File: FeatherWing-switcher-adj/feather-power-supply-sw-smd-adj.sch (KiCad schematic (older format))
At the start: 31 parts, among them J1 Conn_01x12, J2 Conn_01x16, J3 QWIIC, J4 0.1\"x4, J5 5.08mm, Q1 Q_PMOS_GSD, U1 MCP16312MS

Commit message: minor board changes
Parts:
- C2, C3: Voltage (none) -> 35V
- C5, C6: Voltage (none) -> 6.3V
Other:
- moved on the sheet: F1
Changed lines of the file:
@@
 Comment2 "All capacitors are 0603 X7R class unless noted. C2,C3,C5,C6 are 1206, low esr"
 Comment3 "All resistors are 1% 0603"
-Comment4 "Purple text indicate DigiKey part numbers"
+Comment4 "Purple text indicate Digi-Key part numbers"
 $EndDescr
 $Comp
@@
 F 2 "Connector_JST:JST_SH_SM04B-SRSS-TB_1x04-1MP_P1.00mm_Horizontal" H 3300 4750 50  0001 C CNN
 F 3 "https://cdn-shop.adafruit.com/product-files/4328/4328_C13916-001_CCSH-W10-04-BK-RC-A.pdf" H 3300 4750 50  0001 C CNN
-F 4 "455-1804-1-ND" H 3290 5040 30  0000 C CNN "DigiKey_PN"
+F 4 "455-1804-1-ND" H 3290 5040 30  0001 C CNN "DigiKey_PN"
 	1    3300 4750
 	-1   0    0    1
@@
 L Device:Polyfuse_Small F1
 U 1 1 5F5C90E5
-P 3450 2100
-F 0 "F1" V 3550 2100 50  0000 C CNN
-F 1 "24V 1.1A" V 3564 2100 50  0001 C CNN
-F 2 "Fuse:Fuse_1812_4532Metric_Castellated" H 3500 1900 50  0001 L CNN
-F 3 "~" H 3450 2100 50  0001 C CNN
-F 4 "F5632CT-ND" V 3360 2140 30  0001 C CNN "DigiKey-PN"
-F 5 "1812L110/24DR" V 3450 2100 50  0001 C CNN "MPN"
-F 6 "Littelfuse Inc." V 3450 2100 50  0001 C CNN "LittleFuse"
-	1    3450 2100
+P 3475 2100
+F 0 "F1" V 3575 2100 50  0000 C CNN
+F 1 "24V 1.1A" V 3589 2100 50  0001 C CNN
+F 2 "Fuse:Fuse_1812_4532Metric_Castellated" H 3525 1900 50  0001 L CNN
+F 3 "~" H 3475 2100 50  0001 C CNN
+F 4 "F5632CT-ND" V 3385 2140 30  0001 C CNN "DigiKey-PN"
+F 5 "1812L110/24DR" V 3475 2100 50  0001 C CNN "MPN"
+F 6 "Littelfuse Inc." V 3475 2100 50  0001 C CNN "LittleFuse"
+	1    3475 2100
 	0    -1   -1   0
 $EndComp
@@
 U 1 1 5F8EC01A
 P 5000 2200
-F 0 "R1" V 4850 2200 50  0000 C CNN
-F 1 "1M" V 4920 2200 50  0000 C CNN
+F 0 "R1" V 4925 2200 50  0000 C CNN
+F 1 "1M" V 4850 2200 50  0000 C CNN
 F 2 "Resistor_SMD:R_0603_1608Metric_Pad1.05x0.95mm_HandSolder" H 5000 2200 50  0001 C CNN
 F 3 "~" H 5000 2200 50  0001 C CNN
@@
 	3300 2000 3300 2100
 Wire Wire Line
-	3300 2100 3350 2100
-Wire Wire Line
-	3550 2100 3650 2100
+	3300 2100 3375 2100
+Wire Wire Line
+	3575 2100 3650 2100
 $Comp
 L Device:Q_PMOS_GSD Q1
@@
 F 6 "587-3007-1-ND" H 4350 2550 50  0001 C CNN "Digi-Key_PN"
 F 7 "Digi-Key" H 4350 2550 50  0001 C CNN "Vendor"
+F 8 "35V" H 4250 2350 50  0000 C CNN "Voltage"
 	1    4350 2550
 	1    0    0    -1
@@
 F 6 "587-1346-1-ND" H 7050 2550 50  0001 C CNN "Digi-Key_PN"
 F 7 "Digi-Key" H 7050 2550 50  0001 C CNN "Vendor"
+F 8 "6.3V" H 6950 2350 50  0000 C CNN "Voltage"
 	1    7050 2550
-	1    0    0    -1
-$EndComp
-$Comp
-L Device:C_Small C6
-U 1 1 5F96DAE5
-P 7350 2550
-F 0 "C6" H 7150 2550 50  0000 L CNN
-F 1 "10uF" H 7150 2450 50  0000 L CNN
-F 2 "Capacitor_SMD:C_1206_3216Metric_Pad1.42x1.75mm_HandSolder" H 7350 2550 50  0001 C CNN
-F 3 "~" H 7350 2550 50  0001 C CNN
-F 4 "Taiyo Yuden" H 7350 2550 50  0001 C CNN "Manufacturer"
-F 5 "JMK316B7106KL-T" H 7350 2550 50  0001 C CNN "MPN"
-F 6 "587-1346-1-ND" H 7350 2550 50  0001 C CNN "Digi-Key_PN"
-F 7 "Digi-Key" H 7350 2550 50  0001 C CNN "Vendor"
-	1    7350 2550
-	1    0    0    -1
-$EndComp
-$Comp
-L Device:C_Small C3
-U 1 1 5F96F936
-P 4650 2550
-F 0 "C3" H 4450 2550 50  0000 L CNN
-F 1 "10uF" H 4450 2450 50  0000 L CNN
-F 2 "Capacitor_SMD:C_1206_3216Metric_Pad1.42x1.75mm_HandSolder" H 4650 2550 50  0001 C CNN
-F 3 "~" H 4650 2550 50  0001 C CNN
-F 4 "Taiyo Yuden" H 4650 2550 50  0001 C CNN "Manufacturer"
-F 5 "JMK316B7106KL-T" H 4650 2550 50  0001 C CNN "MPN"
-F 6 "587-3007-1-ND" H 4650 2550 50  0001 C CNN "Digi-Key_PN"
-F 7 "Digi-Key" H 4650 2550 50  0001 C CNN "Vendor"
-	1    4650 2550
 	1    0    0    -1
 $EndComp
@@
 P 4100 2300
 F 0 "D2" V 4100 2350 50  0000 L CNN
-F 1 "10V" H 4040 2220 50  0001 L CNN
+F 1 "10V" V 4200 2300 50  0000 L CNN
 F 2 "Diode_SMD:D_SOD-323" V 4100 2300 50  0001 C CNN
 F 3 "https://www.onsemi.com/pub/Collateral/MM3Z2V4ST1-D.PDF" V 4100 2300 50  0001 C CNN
@@
 F 3 "~" H 3350 5650 50  0001 C CNN
 F 4 "1729128" H 3350 5650 50  0001 C CNN "MPN"
-F 5 "277-1247-ND " H 3420 5810 30  0000 C CNN "Digikey_PN"
+F 5 "277-1247-ND " H 3420 5810 30  0001 C CNN "Digikey_PN"
 F 6 "Phoenix Contact" H 3350 5650 50  0001 C CNN "Manufacturer"
 	1    3350 5650
@@
 Text GLabel 7615 3900 2    50   Input ~ 0
 +5V
+$Comp
+L Device:C_Small C3
+U 1 1 5F852525
+P 4650 2550
+F 0 "C3" H 4450 2550 50  0000 L CNN
+F 1 "10uF" H 4450 2450 50  0000 L CNN
+F 2 "Capacitor_SMD:C_1206_3216Metric_Pad1.42x1.75mm_HandSolder" H 4650 2550 50  0001 C CNN
+F 3 "~" H 4650 2550 50  0001 C CNN
+F 4 "Taiyo Yuden" H 4650 2550 50  0001 C CNN "Manufacturer"
+F 5 "JMK316B7106KL-T" H 4650 2550 50  0001 C CNN "MPN"
+F 6 "587-3007-1-ND" H 4650 2550 50  0001 C CNN "Digi-Key_PN"
+F 7 "Digi-Key" H 4650 2550 50  0001 C CNN "Vendor"
+F 8 "35V" H 4550 2350 50  0000 C CNN "Voltage"
+	1    4650 2550
+	1    0    0    -1
+$EndComp
+$Comp
+L Device:C_Small C6
+U 1 1 5F853B4B
+P 7350 2550
+F 0 "C6" H 7150 2550 50  0000 L CNN
+F 1 "10uF" H 7150 2450 50  0000 L CNN
+F 2 "Capacitor_SMD:C_1206_3216Metric_Pad1.42x1.75mm_HandSolder" H 7350 2550 50  0001 C CNN
+F 3 "~" H 7350 2550 50  0001 C CNN
+F 4 "Taiyo Yuden" H 7350 2550 50  0001 C CNN "Manufacturer"
+F 5 "JMK316B7106KL-T" H 7350 2550 50  0001 C CNN "MPN"
+F 6 "587-1346-1-ND" H 7350 2550 50  0001 C CNN "Digi-Key_PN"
+F 7 "Digi-Key" H 7350 2550 50  0001 C CNN "Vendor"
+F 8 "6.3V" H 7250 2350 50  0000 C CNN "Voltage"
+	1    7350 2550
+	1    0    0    -1
+$EndComp
 $EndSCHEMATC

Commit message: minor board/schematic changes
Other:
- note added: "5V OUT @ 1A"
- note added: "Cut JP1 to disable\nvoltage monitor on A1"
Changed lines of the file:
@@
 	1    0    0    -1
 $EndComp
+Text Notes 3500 3900 0    30   Italic 0
+Cut JP1 to disable\nvoltage monitor on A1
+Text Notes 7625 2125 0    50   ~ 0
+5V OUT @ 1A
 $EndSCHEMATC

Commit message: minor updates to bom and layout
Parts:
- C2, C3: Digi-Key_PN 587-3007-1-ND -> 1276-6767-1-ND; MPN JMK316B7106KL-T -> CL31B106KBHNNNE; Manufacturer Taiyo Yuden -> Samsung Electro-Mechanics; Voltage 35V -> 50V
- C5, C6: footprint Capacitor_SMD:C_1206_3216Metric_Pad1.42x1.75mm_HandSolder -> Capacitor_SMD:C_0805_2012Metric_Pad1.15x1.40mm_HandSolder; Digi-Key_PN 587-1346-1-ND -> 1276-2872-1-ND; MPN JMK316B7106KL-T -> CL21B106KOQNNNE; Manufacturer Taiyo Yuden -> Samsung Electro-Mechanics; Voltage 6.3V -> 16V
- R1: Digi-Key_PN (none) -> CR0603-FX-1004ELFCT-ND; DigiKey_PN ‎P20138CT-ND‎ -> (none); MPN (none) -> CR0603-FX-1004ELF; Manufacturer (none) -> Bourns Inc.; Vendor (none) -> Digi-Key
- R2: value 150 -> 330; Digi-Key_PN (none) -> CR0603-FX-3300ELFTR-ND; MPN (none) -> CR0603-FX-3300ELF; Manufacturer (none) -> Bourns Inc.; Vendor (none) -> Digi-Key
- R3: Digi-Key_PN (none) -> CR0603-FX-5602ELFCT-ND; DigiKey_PN ‎P20138CT-ND‎ -> (none); MPN (none) -> CR0603-FX-5602ELF; Manufacturer (none) -> Bourns Inc.; Vendor (none) -> Digi-Key
- R4, R5: Digi-Key_PN (none) -> CR0603-FX-1002ELFCT-ND; DigiKey_PN ‎P20138CT-ND‎ -> (none); MPN (none) -> CR0603-FX-1002ELF; Manufacturer (none) -> Bourns Inc.; Vendor (none) -> Digi-Key
- R6: value 100K -> 1M; Digi-Key_PN (none) -> CR0603-FX-1004ELFCT-ND; DigiKey_PN ‎P20138CT-ND‎ -> (none); MPN (none) -> CR0603-FX-1004ELF; Manufacturer (none) -> Bourns Inc.; Vendor (none) -> Digi-Key
- R7: value 10K -> 100K; Digi-Key_PN (none) -> CR0603-FX-1003ELFCT-ND; DigiKey_PN P20072CT-ND‎ -> (none); MPN (none) -> CR0603-FX-1003ELF; Manufacturer (none) -> Bourns Inc.; Vendor (none) -> Digi-Key
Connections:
- net A1: now also R6.2; no longer R6.1
- net at JP1.2 (B): now also R6.1; no longer R6.2
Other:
- note added: "Vf=2.1V\nIf=(5-2.1V)/330\nIf= 8.9mA"
- note removed: "Vf=2.1V\nIf=(5-2.1V)/150\nIf= 19mA"
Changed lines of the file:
@@
 F 2 "Resistor_SMD:R_0603_1608Metric_Pad1.05x0.95mm_HandSolder" H 6650 2750 50  0001 C CNN
 F 3 "~" H 6650 2750 50  0001 C CNN
-F 4 "‎P20138CT-ND‎" V 6650 2750 50  0001 C CNN "DigiKey_PN"
+F 4 "Bourns Inc." H 6650 2750 50  0001 C CNN "Manufacturer"
+F 5 "CR0603-FX-1002ELF" H 6650 2750 50  0001 C CNN "MPN"
+F 6 "CR0603-FX-1002ELFCT-ND" H 6650 2750 50  0001 C CNN "Digi-Key_PN"
+F 7 "Digi-Key" H 6650 2750 50  0001 C CNN "Vendor"
 	1    6650 2750
 	1    0    0    -1
@@
 	1    4200 4050
 	1    0    0    -1
-$EndComp
-$Comp
-L Device:R_Small R6
-U 1 1 5F47540B
-P 4050 3700
-F 0 "R6" V 3920 3700 50  0000 C CNN
-F 1 "100K" V 3980 3700 50  0000 C CNN
-F 2 "Resistor_SMD:R_0603_1608Metric_Pad1.05x0.95mm_HandSolder" H 4050 3700 50  0001 C CNN
-F 3 "~" H 4050 3700 50  0001 C CNN
-F 4 "‎P20138CT-ND‎" V 4050 3700 50  0001 C CNN "DigiKey_PN"
-	1    4050 3700
-	0    1    1    0
 $EndComp
 $Comp
@@
 P 7700 2400
 F 0 "R2" H 7750 2430 50  0000 L CNN
-F 1 "150" H 7750 2360 50  0000 L CNN
+F 1 "330" H 7750 2360 50  0000 L CNN
 F 2 "Resistor_SMD:R_0603_1608Metric_Pad1.05x0.95mm_HandSolder" H 7700 2400 50  0001 C CNN
 F 3 "~" H 7700 2400 50  0001 C CNN
+F 4 "Bourns Inc." H 7700 2400 50  0001 C CNN "Manufacturer"
+F 5 "CR0603-FX-3300ELF" H 7700 2400 50  0001 C CNN "MPN"
+F 6 "CR0603-FX-3300ELFTR-ND" H 7700 2400 50  0001 C CNN "Digi-Key_PN"
+F 7 "Digi-Key" H 7700 2400 50  0001 C CNN "Vendor"
 	1    7700 2400
 	1    0    0    -1
@@
 P 5150 2650
 F 0 "C4" H 4950 2650 50  0000 L CNN
-F 1 "1uF" H 4900 2550 50  0000 L CNN
+F 1 "1uF" H 4925 2575 50  0000 L CNN
 F 2 "Capacitor_SMD:C_0603_1608Metric_Pad1.05x0.95mm_HandSolder" H 5150 2650 50  0001 C CNN
 F 3 "~" H 5150 2650 50  0001 C CNN
@@
 F 2 "Resistor_SMD:R_0603_1608Metric_Pad1.05x0.95mm_HandSolder" H 5000 2200 50  0001 C CNN
 F 3 "~" H 5000 2200 50  0001 C CNN
-F 4 "‎P20138CT-ND‎" V 5000 2200 50  0001 C CNN "DigiKey_PN"
+F 4 "Bourns Inc." H 5000 2200 50  0001 C CNN "Manufacturer"
+F 5 "CR0603-FX-1004ELF" H 5000 2200 50  0001 C CNN "MPN"
+F 6 "CR0603-FX-1004ELFCT-ND" H 5000 2200 50  0001 C CNN "Digi-Key_PN"
+F 7 "Digi-Key" H 5000 2200 50  0001 C CNN "Vendor"
 	1    5000 2200
 	0    -1   -1   0
@@
 F 2 "Capacitor_SMD:C_1206_3216Metric_Pad1.42x1.75mm_HandSolder" H 4350 2550 50  0001 C CNN
 F 3 "~" H 4350 2550 50  0001 C CNN
-F 4 "Taiyo Yuden" H 4350 2550 50  0001 C CNN "Manufacturer"
-F 5 "JMK316B7106KL-T" H 4350 2550 50  0001 C CNN "MPN"
-F 6 "587-3007-1-ND" H 4350 2550 50  0001 C CNN "Digi-Key_PN"
+F 4 "Samsung Electro-Mechanics" H 4350 2550 50  0001 C CNN "Manufacturer"
+F 5 "CL31B106KBHNNNE" H 4350 2550 50  0001 C CNN "MPN"
+F 6 "1276-6767-1-ND" H 4350 2550 50  0001 C CNN "Digi-Key_PN"
 F 7 "Digi-Key" H 4350 2550 50  0001 C CNN "Vendor"
-F 8 "35V" H 4250 2350 50  0000 C CNN "Voltage"
+F 8 "50V" H 4250 2350 50  0000 C CNN "Voltage"
 	1    4350 2550
 	1    0    0    -1
@@
 F 2 "Resistor_SMD:R_0603_1608Metric_Pad1.05x0.95mm_HandSolder" H 6650 2400 50  0001 C CNN
 F 3 "~" H 6650 2400 50  0001 C CNN
-F 4 "‎P20138CT-ND‎" V 6650 2400 50  0001 C CNN "DigiKey_PN"
+F 4 "Bourns Inc." H 6650 2400 50  0001 C CNN "Manufacturer"
+F 5 "CR0603-FX-5602ELF" H 6650 2400 50  0001 C CNN "MPN"
+F 6 "CR0603-FX-5602ELFCT-ND" H 6650 2400 50  0001 C CNN "Digi-Key_PN"
+F 7 "Digi-Key" H 6650 2400 50  0001 C CNN "Vendor"
 	1    6650 2400
 	1    0    0    -1
@@
 F 0 "C5" H 6850 2550 50  0000 L CNN
 F 1 "10uF" H 6850 2450 50  0000 L CNN
-F 2 "Capacitor_SMD:C_1206_3216Metric_Pad1.42x1.75mm_HandSolder" H 7050 2550 50  0001 C CNN
+F 2 "Capacitor_SMD:C_0805_2012Metric_Pad1.15x1.40mm_HandSolder" H 7050 2550 50  0001 C CNN
 F 3 "~" H 7050 2550 50  0001 C CNN
-F 4 "Taiyo Yuden" H 7050 2550 50  0001 C CNN "Manufacturer"
-F 5 "JMK316B7106KL-T" H 7050 2550 50  0001 C CNN "MPN"
-F 6 "587-1346-1-ND" H 7050 2550 50  0001 C CNN "Digi-Key_PN"
+F 4 "Samsung Electro-Mechanics" H 7050 2550 50  0001 C CNN "Manufacturer"
+F 5 "CL21B106KOQNNNE" H 7050 2550 50  0001 C CNN "MPN"
+F 6 "1276-2872-1-ND" H 7050 2550 50  0001 C CNN "Digi-Key_PN"
 F 7 "Digi-Key" H 7050 2550 50  0001 C CNN "Vendor"
-F 8 "6.3V" H 6950 2350 50  0000 C CNN "Voltage"
+F 8 "16V" H 6950 2350 50  0000 C CNN "Voltage"
 	1    7050 2550
 	1    0    0    -1
@@
 Wire Wire Line
 	4100 2100 4250 2100
-$Comp
-L Device:R_Small R4
-U 1 1 5F98493E
-P 3850 2700
-F 0 "R4" V 3720 2700 50  0000 C CNN
-F 1 "10K" V 3780 2700 50  0000 C CNN
-F 2 "Resistor_SMD:R_0603_1608Metric_Pad1.05x0.95mm_HandSolder" H 3850 2700 50  0001 C CNN
-F 3 "~" H 3850 2700 50  0001 C CNN
-F 4 "‎P20138CT-ND‎" V 3850 2700 50  0001 C CNN "DigiKey_PN"
-	1    3850 2700
-	1    0    0    -1
-$EndComp
 Wire Wire Line
 	3850 2500 3850 2600
@@
 	6300 1900 6350 1900
 Text Notes 7750 2900 0    30   ~ 0
-Vf=2.1V\nIf=(5-2.1V)/150\nIf= 19mA
+Vf=2.1V\nIf=(5-2.1V)/330\nIf= 8.9mA
 $Comp
 L mcp16311ms:MCP16312MS U1
@@
 U 1 1 5F475325
 P 4200 3900
-F 0 "R7" H 4060 3935 50  0000 L CNN
-F 1 "10K" H 4020 3870 50  0000 L CNN
+F 0 "R7" H 4250 3925 50  0000 L CNN
+F 1 "100K" H 4250 3850 50  0000 L CNN
 F 2 "Resistor_SMD:R_0603_1608Metric_Pad1.05x0.95mm_HandSolder" H 4200 3900 50  0001 C CNN
 F 3 "~" H 4200 3900 50  0001 C CNN
-F 4 "P20072CT-ND‎" H 4200 3900 50  0001 C CNN "DigiKey_PN"
+F 4 "Bourns Inc." H 4200 3900 50  0001 C CNN "Manufacturer"
+F 5 "CR0603-FX-1003ELF" H 4200 3900 50  0001 C CNN "MPN"
+F 6 "CR0603-FX-1003ELFCT-ND" H 4200 3900 50  0001 C CNN "Digi-Key_PN"
+F 7 "Digi-Key" H 4200 3900 50  0001 C CNN "Vendor"
 	1    4200 3900
 	1    0    0    -1
@@
 Text GLabel 7615 3900 2    50   Input ~ 0
 +5V
+Text Notes 3500 3900 0    30   Italic 0
+Cut JP1 to disable\nvoltage monitor on A1
+Text Notes 7625 2125 0    50   ~ 0
+5V OUT @ 1A
+$Comp
+L Device:R_Small R6
+U 1 1 5F8CA057
+P 4050 3700
+F 0 "R6" V 4125 3700 50  0000 C CNN
+F 1 "1M" V 4200 3700 50  0000 C CNN
+F 2 "Resistor_SMD:R_0603_1608Metric_Pad1.05x0.95mm_HandSolder" H 4050 3700 50  0001 C CNN
+F 3 "~" H 4050 3700 50  0001 C CNN
+F 4 "Bourns Inc." H 4050 3700 50  0001 C CNN "Manufacturer"
+F 5 "CR0603-FX-1004ELF" H 4050 3700 50  0001 C CNN "MPN"
+F 6 "CR0603-FX-1004ELFCT-ND" H 4050 3700 50  0001 C CNN "Digi-Key_PN"
+F 7 "Digi-Key" H 4050 3700 50  0001 C CNN "Vendor"
+	1    4050 3700
+	0    -1   -1   0
+$EndComp
 $Comp
 L Device:C_Small C3
-U 1 1 5F852525
+U 1 1 5F8CEF7B
 P 4650 2550
 F 0 "C3" H 4450 2550 50  0000 L CNN
@@
 F 2 "Capacitor_SMD:C_1206_3216Metric_Pad1.42x1.75mm_HandSolder" H 4650 2550 50  0001 C CNN
 F 3 "~" H 4650 2550 50  0001 C CNN
-F 4 "Taiyo Yuden" H 4650 2550 50  0001 C CNN "Manufacturer"
-F 5 "JMK316B7106KL-T" H 4650 2550 50  0001 C CNN "MPN"
-F 6 "587-3007-1-ND" H 4650 2550 50  0001 C CNN "Digi-Key_PN"
+F 4 "Samsung Electro-Mechanics" H 4650 2550 50  0001 C CNN "Manufacturer"
+F 5 "CL31B106KBHNNNE" H 4650 2550 50  0001 C CNN "MPN"
+F 6 "1276-6767-1-ND" H 4650 2550 50  0001 C CNN "Digi-Key_PN"
 F 7 "Digi-Key" H 4650 2550 50  0001 C CNN "Vendor"
-F 8 "35V" H 4550 2350 50  0000 C CNN "Voltage"
+F 8 "50V" H 4550 2350 50  0000 C CNN "Voltage"
 	1    4650 2550
 	1    0    0    -1
@@
 $Comp
 L Device:C_Small C6
-U 1 1 5F853B4B
+U 1 1 5F8D1B41
 P 7350 2550
 F 0 "C6" H 7150 2550 50  0000 L CNN
 F 1 "10uF" H 7150 2450 50  0000 L CNN
-F 2 "Capacitor_SMD:C_1206_3216Metric_Pad1.42x1.75mm_HandSolder" H 7350 2550 50  0001 C CNN
+F 2 "Capacitor_SMD:C_0805_2012Metric_Pad1.15x1.40mm_HandSolder" H 7350 2550 50  0001 C CNN
 F 3 "~" H 7350 2550 50  0001 C CNN
-F 4 "Taiyo Yuden" H 7350 2550 50  0001 C CNN "Manufacturer"
-F 5 "JMK316B7106KL-T" H 7350 2550 50  0001 C CNN "MPN"
-F 6 "587-1346-1-ND" H 7350 2550 50  0001 C CNN "Digi-Key_PN"
+F 4 "Samsung Electro-Mechanics" H 7350 2550 50  0001 C CNN "Manufacturer"
+F 5 "CL21B106KOQNNNE" H 7350 2550 50  0001 C CNN "MPN"
+F 6 "1276-2872-1-ND" H 7350 2550 50  0001 C CNN "Digi-Key_PN"
 F 7 "Digi-Key" H 7350 2550 50  0001 C CNN "Vendor"
-F 8 "6.3V" H 7250 2350 50  0000 C CNN "Voltage"
+F 8 "16V" H 7250 2350 50  0000 C CNN "Voltage"
 	1    7350 2550
 	1    0    0    -1
 $EndComp
-Text Notes 3500 3900 0    30   Italic 0
-Cut JP1 to disable\nvoltage monitor on A1
-Text Notes 7625 2125 0    50   ~ 0
-5V OUT @ 1A
+$Comp
+L Device:R_Small R4
+U 1 1 5F8DDF4C
+P 3850 2700
+F 0 "R4" V 3720 2700 50  0000 C CNN
+F 1 "10K" V 3780 2700 50  0000 C CNN
+F 2 "Resistor_SMD:R_0603_1608Metric_Pad1.05x0.95mm_HandSolder" H 3850 2700 50  0001 C CNN
+F 3 "~" H 3850 2700 50  0001 C CNN
+F 4 "Bourns Inc." H 3850 2700 50  0001 C CNN "Manufacturer"
+F 5 "CR0603-FX-1002ELF" H 3850 2700 50  0001 C CNN "MPN"
+F 6 "CR0603-FX-1002ELFCT-ND" H 3850 2700 50  0001 C CNN "Digi-Key_PN"
+F 7 "Digi-Key" H 3850 2700 50  0001 C CNN "Vendor"
+	1    3850 2700
+	1    0    0    -1
+$EndComp
 $EndSCHEMATC

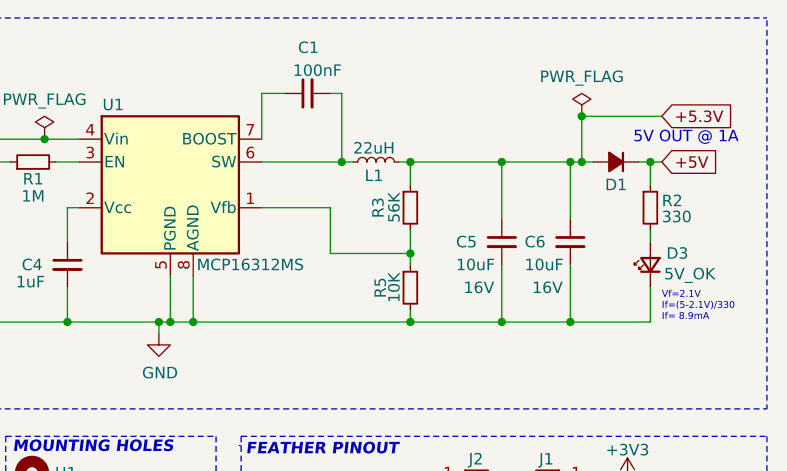
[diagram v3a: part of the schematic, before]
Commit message: update fb res val and inductor val
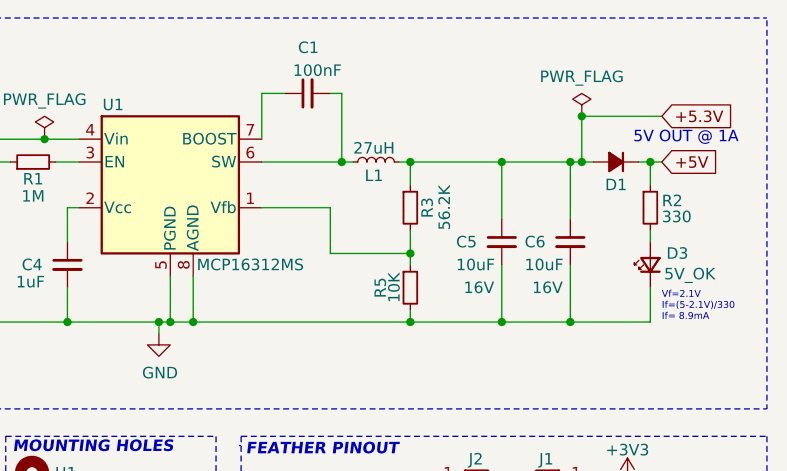
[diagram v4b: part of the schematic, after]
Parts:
- L1: value 22uH -> 27uH; Digi-Key_PN SRR7045-220MCT-ND -> SRR7045-270MCT-ND; MPN SRR7045-220M -> SRR7045-270M
- R3: value 56K -> 56.2K; Digi-Key_PN CR0603-FX-5602ELFCT-ND -> 541-56.2KHCT-ND; MPN CR0603-FX-5602ELF -> CRCW060356K2FKEA; Manufacturer Bourns Inc. -> Vishay Dale
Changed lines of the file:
@@
 P 6500 2200
 F 0 "L1" V 6440 2250 50  0000 R CNN
-F 1 "22uH" V 6560 2300 50  0000 R CNN
+F 1 "27uH" V 6560 2300 50  0000 R CNN
 F 2 "FeatherWing-switcher-adj:SRR7045-220M" H 6500 2200 50  0001 C CNN
 F 3 "https://www.bourns.com/docs/Product-Datasheets/SRR7045.pdf" H 6500 2200 50  0001 C CNN
 F 4 "Bourns Inc." H 6500 2200 50  0001 C CNN "Manufacturer"
-F 5 "SRR7045-220M" H 6500 2200 50  0001 C CNN "MPN"
-F 6 "SRR7045-220MCT-ND" H 6500 2200 50  0001 C CNN "Digi-Key_PN"
+F 5 "SRR7045-270M" H 6500 2200 50  0001 C CNN "MPN"
+F 6 "SRR7045-270MCT-ND" H 6500 2200 50  0001 C CNN "Digi-Key_PN"
 F 7 "Digi-Key" H 6500 2200 50  0001 C CNN "Vendor"
 	1    6500 2200
@@
 U 1 1 5F4EB99E
 P 6650 2400
-F 0 "R3" V 6510 2400 50  0000 C CNN
-F 1 "56K" V 6580 2400 50  0000 C CNN
+F 0 "R3" V 6725 2400 50  0000 C CNN
+F 1 "56.2K" V 6800 2400 50  0000 C CNN
 F 2 "Resistor_SMD:R_0603_1608Metric_Pad1.05x0.95mm_HandSolder" H 6650 2400 50  0001 C CNN
 F 3 "~" H 6650 2400 50  0001 C CNN
-F 4 "Bourns Inc." H 6650 2400 50  0001 C CNN "Manufacturer"
-F 5 "CR0603-FX-5602ELF" H 6650 2400 50  0001 C CNN "MPN"
-F 6 "CR0603-FX-5602ELFCT-ND" H 6650 2400 50  0001 C CNN "Digi-Key_PN"
+F 4 "Vishay Dale" H 6650 2400 50  0001 C CNN "Manufacturer"
+F 5 "CRCW060356K2FKEA" H 6650 2400 50  0001 C CNN "MPN"
+F 6 "541-56.2KHCT-ND" H 6650 2400 50  0001 C CNN "Digi-Key_PN"
 F 7 "Digi-Key" H 6650 2400 50  0001 C CNN "Vendor"
 	1    6650 2400

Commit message: update inductor and boms
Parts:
- L1: footprint FeatherWing-switcher-adj:SRR7045-220M -> FeatherWing-switcher-adj:ASPI-6045S-270; Digi-Key_PN SRR7045-270MCT-ND -> ASPI-6045S-270M-TCT-ND; MPN SRR7045-270M -> ASPI-6045S-270M-T; Manufacturer Bourns Inc. -> Abracon LLC
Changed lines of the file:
@@
 F 0 "L1" V 6440 2250 50  0000 R CNN
 F 1 "27uH" V 6560 2300 50  0000 R CNN
-F 2 "FeatherWing-switcher-adj:SRR7045-220M" H 6500 2200 50  0001 C CNN
-F 3 "https://www.bourns.com/docs/Product-Datasheets/SRR7045.pdf" H 6500 2200 50  0001 C CNN
-F 4 "Bourns Inc." H 6500 2200 50  0001 C CNN "Manufacturer"
-F 5 "SRR7045-270M" H 6500 2200 50  0001 C CNN "MPN"
-F 6 "SRR7045-270MCT-ND" H 6500 2200 50  0001 C CNN "Digi-Key_PN"
+F 2 "FeatherWing-switcher-adj:ASPI-6045S-270" H 6500 2200 50  0001 C CNN
+F 3 "" H 6500 2200 50  0001 C CNN
+F 4 "Abracon LLC" H 6500 2200 50  0001 C CNN "Manufacturer"
+F 5 "ASPI-6045S-270M-T" H 6500 2200 50  0001 C CNN "MPN"
+F 6 "ASPI-6045S-270M-TCT-ND" H 6500 2200 50  0001 C CNN "Digi-Key_PN"
 F 7 "Digi-Key" H 6500 2200 50  0001 C CNN "Vendor"
 	1    6500 2200
